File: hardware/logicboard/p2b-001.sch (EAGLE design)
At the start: 54 parts, among them IC1 74LS06N, IC2 4066N, J1 MKR, J2 GPIO, J3 Vcc, J4 RLY, J5 SPI, J7 DIN5, J8 DIN5, J9 DIN5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

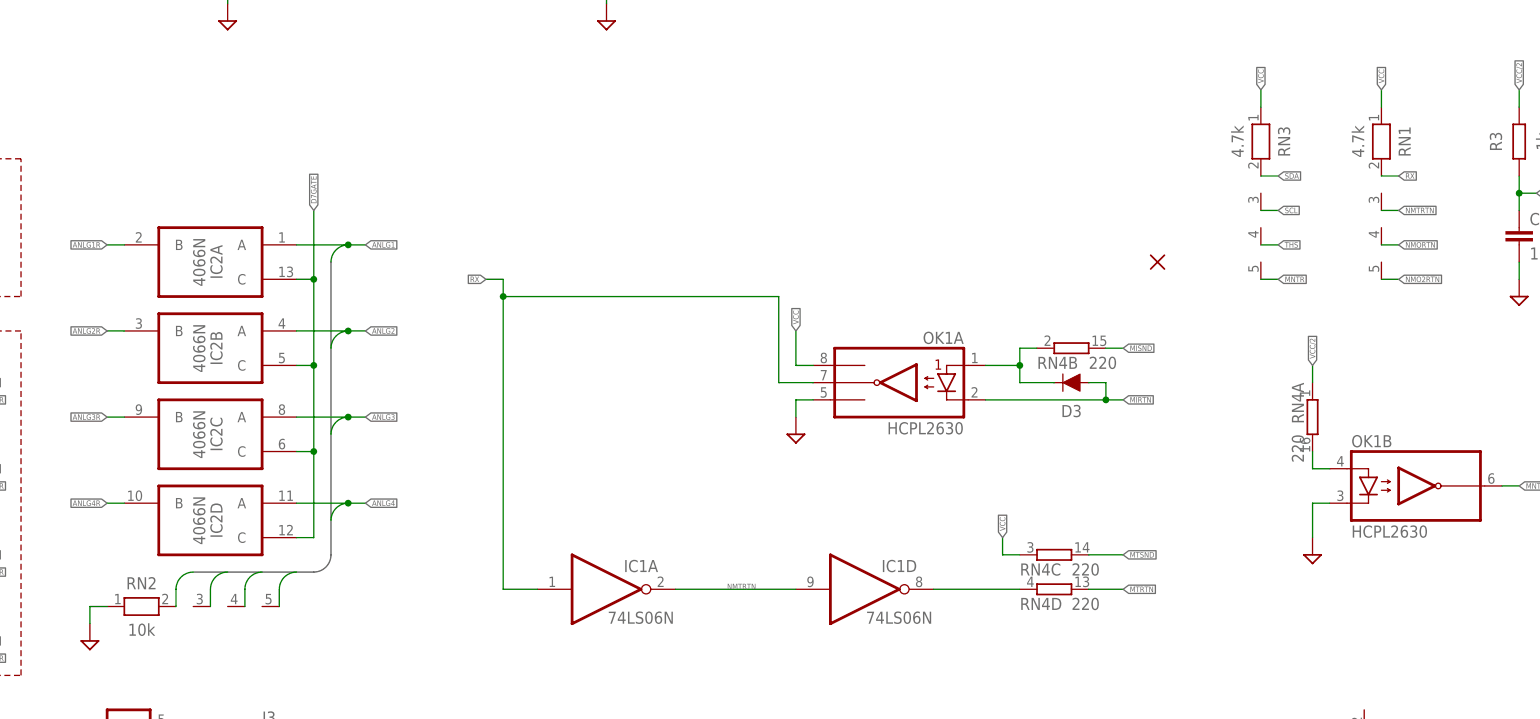
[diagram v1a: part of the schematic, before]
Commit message: Swapped RN1 and RN2.
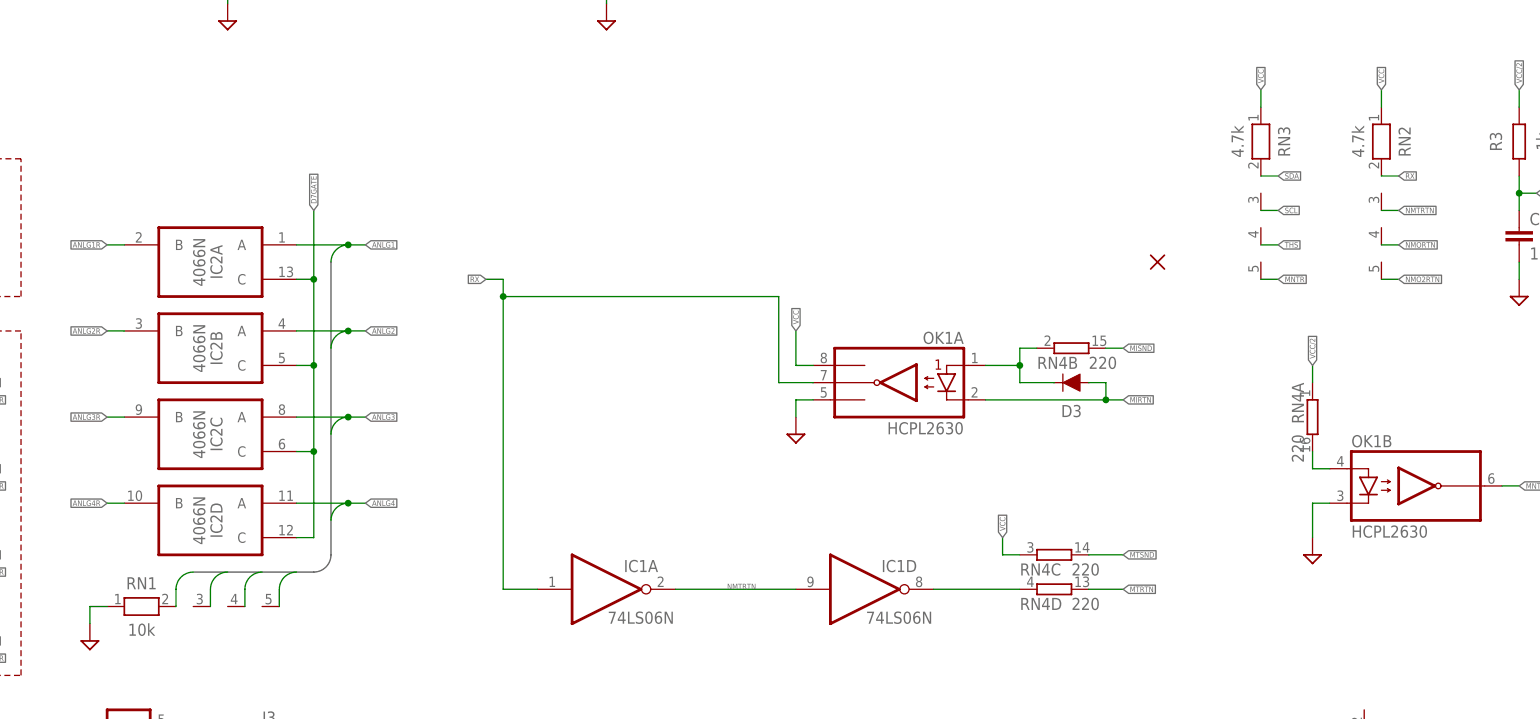
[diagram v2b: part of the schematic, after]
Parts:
- RN1: value 4.7k -> 10k
- RN2: value 10k -> 4.7k
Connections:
- net ANLG1: now also RN1.2; no longer RN2.2
- net ANLG2: now also RN1.3; no longer RN2.3
- net ANLG3: now also RN1.4; no longer RN2.4
- net ANLG4: now also RN1.5; no longer RN2.5
- net GND: now also RN1.1; no longer RN2.1
- net NMO2RTN: now also RN2.5; no longer RN1.5
- net NMORTN: now also RN2.4; no longer RN1.4
- net NMTRTN: now also RN2.3; no longer RN1.3
- net RX: now also RN2.2; no longer RN1.2
- net VCC: now also RN2.1; no longer RN1.1
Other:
- moved on the sheet: RN1, RN2
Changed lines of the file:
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@@
 <part name="R2" library="resistor" library_urn="urn:adsk.eagle:library:348" deviceset="R-EU_" device="0204/5" package3d_urn="urn:adsk.eagle:package:23488/1" value="47k"/>
 <part name="SUPPLY7" library="supply2" deviceset="GND" device=""/>
-<part name="RN2" library="resistor-net" library_urn="urn:adsk.eagle:library:343" deviceset="RN04" device="" package3d_urn="urn:adsk.eagle:package:24976/1" value="10k"/>
+<part name="RN1" library="resistor-net" library_urn="urn:adsk.eagle:library:343" deviceset="RN04" device="" package3d_urn="urn:adsk.eagle:package:24976/1" value="10k"/>
 <part name="IC2" library="40xx" library_urn="urn:adsk.eagle:library:80" deviceset="4066" device="N" package3d_urn="urn:adsk.eagle:package:16407/2"/>
 <part name="SUPPLY26" library="supply2" deviceset="GND" device=""/>
@@
 <part name="C10" library="rcl" library_urn="urn:adsk.eagle:library:334" deviceset="C-EU" device="025-024X044" package3d_urn="urn:adsk.eagle:package:23630/1" value="100n"/>
 <part name="SUPPLY44" library="supply2" deviceset="GND" device=""/>
-<part name="RN1" library="resistor-net" library_urn="urn:adsk.eagle:library:343" deviceset="RN04" device="" package3d_urn="urn:adsk.eagle:package:24976/1" value="4.7k"/>
+<part name="RN2" library="resistor-net" library_urn="urn:adsk.eagle:library:343" deviceset="RN04" device="" package3d_urn="urn:adsk.eagle:package:24976/1" value="4.7k"/>
 <part name="SV1" library="con-ml" library_urn="urn:adsk.eagle:library:164" deviceset="ML16LE" device="" package3d_urn="urn:adsk.eagle:package:8682/1"/>
 <part name="H1" library="SparkFun-Hardware" library_urn="urn:adsk.eagle:library:519" deviceset="STAND-OFF" device="" package3d_urn="urn:adsk.eagle:package:38630/1"/>
@@
 </instance>
 <instance part="SUPPLY7" gate="GND" x="137.16" y="172.72" smashed="yes"/>
-<instance part="RN2" gate="1" x="68.58" y="86.36" smashed="yes">
+<instance part="RN1" gate="1" x="68.58" y="86.36" smashed="yes">
 <attribute name="NAME" x="68.58" y="88.9" size="1.778" layer="95" align="bottom-center"/>
 <attribute name="VALUE" x="68.58" y="83.82" size="1.778" layer="96" align="top-center"/>
@@
 </instance>
 <instance part="SUPPLY44" gate="GND" x="271.78" y="132.08" smashed="yes"/>
-<instance part="RN1" gate="1" x="251.46" y="154.94" smashed="yes" rot="R270">
+<instance part="RN2" gate="1" x="251.46" y="154.94" smashed="yes" rot="R270">
 <attribute name="NAME" x="254" y="154.94" size="1.778" layer="95" rot="R270" align="bottom-center"/>
 <attribute name="VALUE" x="248.92" y="154.94" size="1.778" layer="96" rot="R270" align="top-center"/>
@@
 </segment>
 <segment>
-<pinref part="RN2" gate="1" pin="1"/>
+<pinref part="RN1" gate="1" pin="1"/>
 <wire x1="63.5" y1="86.36" x2="60.96" y2="86.36" width="0.1524" layer="91"/>
 <pinref part="SUPPLY23" gate="GND" pin="GND"/>
@@
 </segment>
 <segment>
-<pinref part="RN1" gate="1" pin="1"/>
+<pinref part="RN2" gate="1" pin="1"/>
 <wire x1="251.46" y1="160.02" x2="251.46" y2="162.56" width="0.1524" layer="91"/>
 <label x="251.46" y="162.56" size="0.8128" layer="95" rot="R90" xref="yes"/>
@@
 </segment>
 <segment>
-<pinref part="RN2" gate="1" pin="5"/>
+<pinref part="RN1" gate="1" pin="5"/>
 <wire x1="91.44" y1="91.44" x2="88.9" y2="88.9" width="0.1524" layer="91" curve="90"/>
 <wire x1="88.9" y1="88.9" x2="88.9" y2="86.36" width="0.1524" layer="91"/>
@@
 </segment>
 <segment>
-<pinref part="RN2" gate="1" pin="4"/>
+<pinref part="RN1" gate="1" pin="4"/>
 <wire x1="86.36" y1="91.44" x2="83.82" y2="88.9" width="0.1524" layer="91" curve="90"/>
 <wire x1="83.82" y1="88.9" x2="83.82" y2="86.36" width="0.1524" layer="91"/>
@@
 </segment>
 <segment>
-<pinref part="RN2" gate="1" pin="3"/>
+<pinref part="RN1" gate="1" pin="3"/>
 <wire x1="81.28" y1="91.44" x2="78.74" y2="88.9" width="0.1524" layer="91" curve="90"/>
 <wire x1="78.74" y1="88.9" x2="78.74" y2="86.36" width="0.1524" layer="91"/>
@@
 </segment>
 <segment>
-<pinref part="RN2" gate="1" pin="2"/>
+<pinref part="RN1" gate="1" pin="2"/>
 <wire x1="76.2" y1="91.44" x2="73.66" y2="88.9" width="0.1524" layer="91" curve="90"/>
 <wire x1="73.66" y1="88.9" x2="73.66" y2="86.36" width="0.1524" layer="91"/>
@@
 </segment>
 <segment>
-<pinref part="RN1" gate="1" pin="2"/>
+<pinref part="RN2" gate="1" pin="2"/>
 <wire x1="251.46" y1="149.86" x2="254" y2="149.86" width="0.1524" layer="91"/>
 <label x="254" y="149.86" size="0.8128" layer="95" xref="yes"/>
@@
 </segment>
 <segment>
-<pinref part="RN1" gate="1" pin="3"/>
+<pinref part="RN2" gate="1" pin="3"/>
 <wire x1="251.46" y1="144.78" x2="254" y2="144.78" width="0.1524" layer="91"/>
 <label x="254" y="144.78" size="0.8128" layer="95" xref="yes"/>
@@
 </segment>
 <segment>
-<pinref part="RN1" gate="1" pin="4"/>
+<pinref part="RN2" gate="1" pin="4"/>
 <wire x1="251.46" y1="139.7" x2="254" y2="139.7" width="0.1524" layer="91"/>
 <label x="254" y="139.7" size="0.8128" layer="95" xref="yes"/>
@@
 </segment>
 <segment>
-<pinref part="RN1" gate="1" pin="5"/>
+<pinref part="RN2" gate="1" pin="5"/>
 <wire x1="251.46" y1="134.62" x2="254" y2="134.62" width="0.1524" layer="91"/>
 <label x="254" y="134.62" size="0.8128" layer="95" xref="yes"/>

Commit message: The new test pad.
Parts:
- removed JP7: (no value), pinhead:PINHD-2X8
- added SV3: (no value), con-ml:ML14E
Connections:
- net D7GATE: now also SV3-7.S; no longer JP7.7
- net DTCT1: now also SV3-11.S; no longer JP7.11
- net DTCT2: now also SV3-12.S; no longer JP7.12
- net DTCT3: now also SV3-13.S; no longer JP7.13
- net DTCT4: now also SV3-14.S; no longer JP7.14
- net GND: now also SV3-1.S; no longer JP7.1
- net GPIO1: now also SV3-9.S; no longer JP7.9
- net GPIO2: now also SV3-10.S; no longer JP7.10
- net LED2: no longer JP7.2
- net MNTR: no longer JP7.15
- net RLY: no longer JP7.8
- net RX: now also SV3-3.S; no longer JP7.3
- net SCL: now also SV3-6.S; no longer JP7.6
- net SDA: now also SV3-5.S; no longer JP7.5
- net THS: now also SV3-8.S; no longer JP7.16
- net TX: now also SV3-4.S; no longer JP7.4
- net VCC: now also SV3-2.S

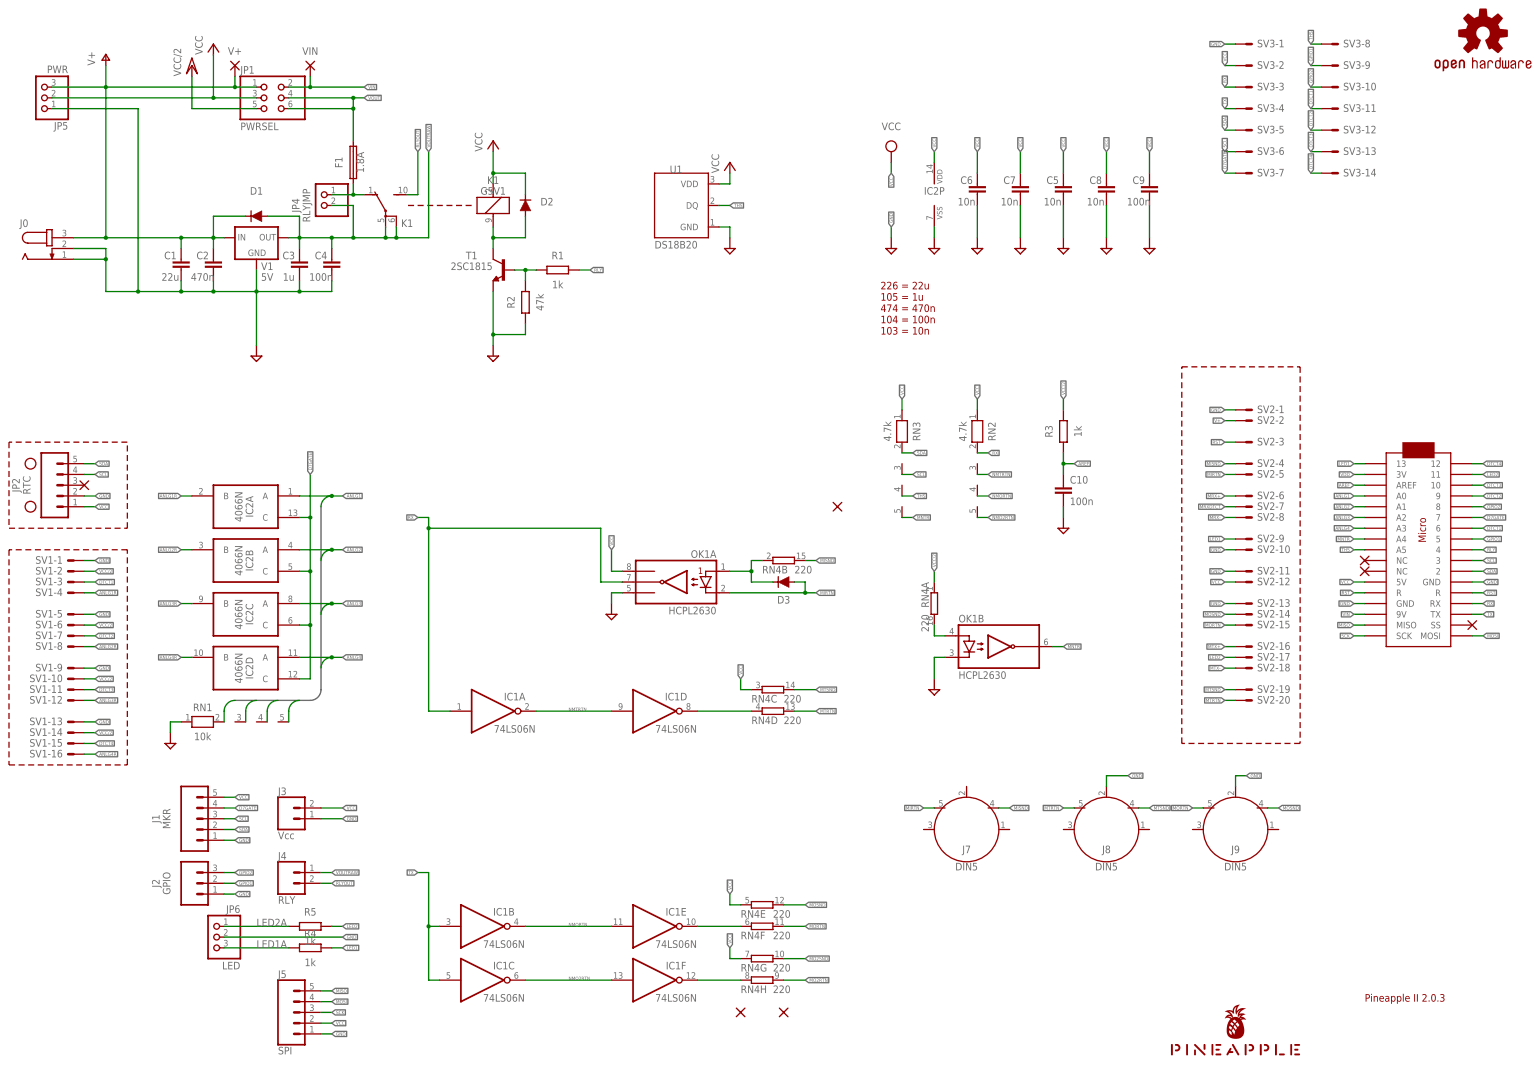
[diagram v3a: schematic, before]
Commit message: Renumbered signal names and silk patterns.
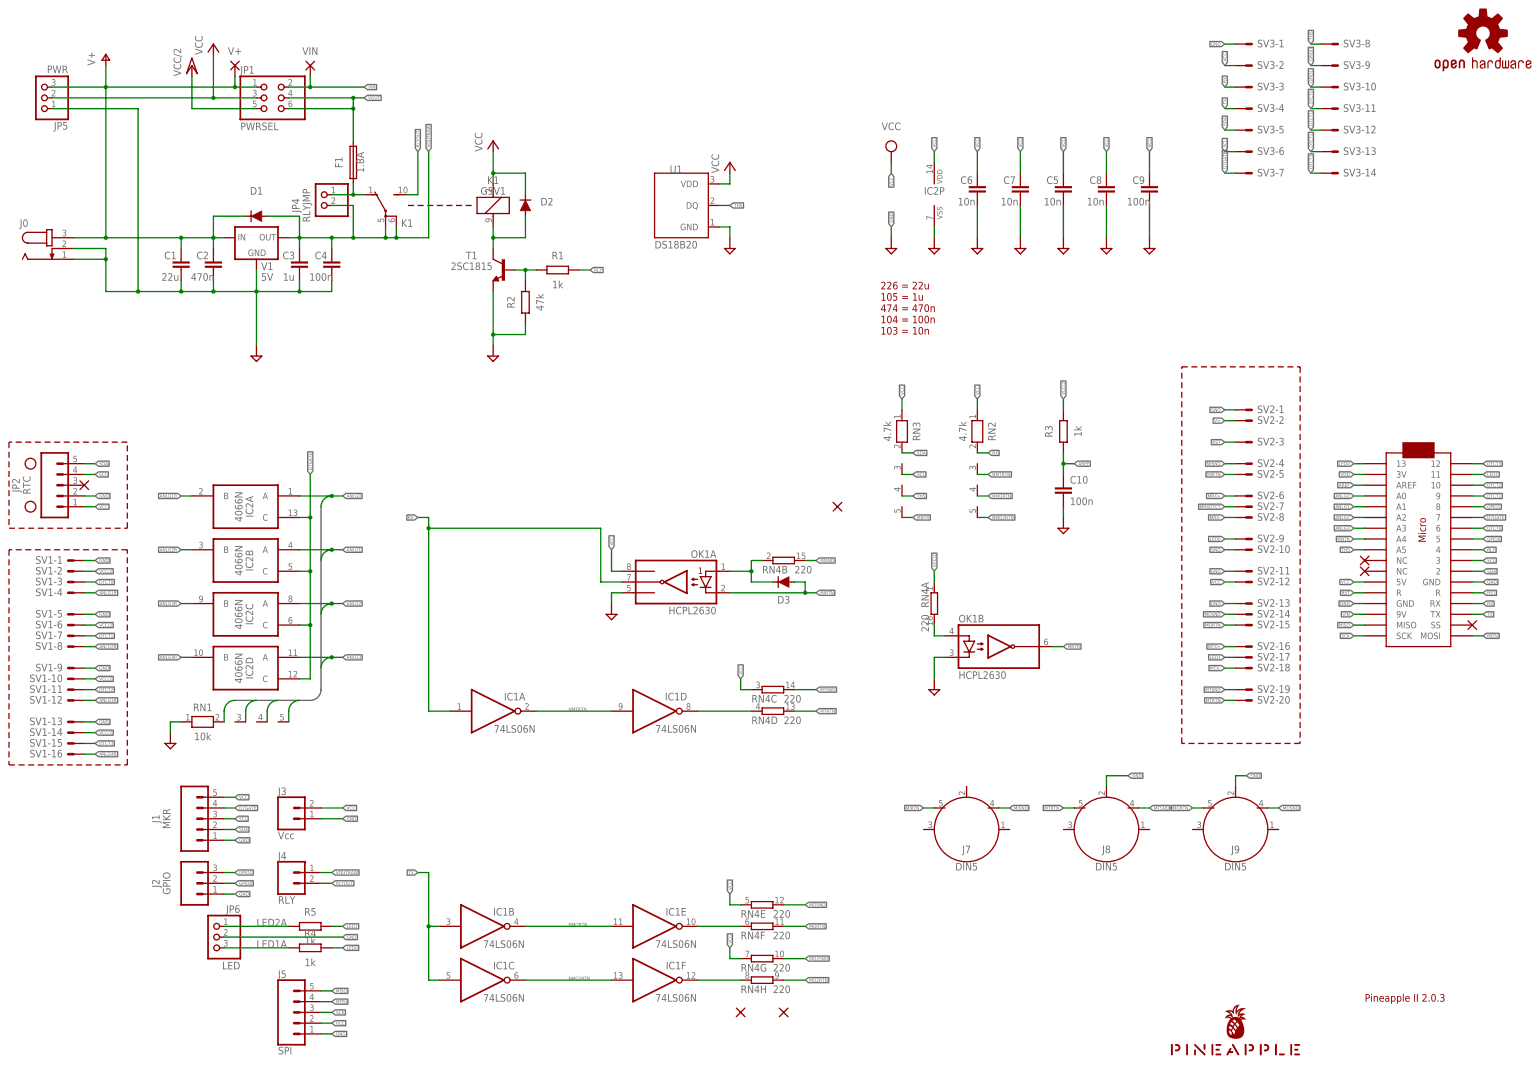
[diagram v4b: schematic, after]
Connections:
- removed net ANLG4: IC2D.A, MC1.A3, RN1.5
- removed net DTCT4: MC1.12, SV1-15.S, SV3-14.S
- removed net GPIO2: J2.3, MC1.8, SV3-10.S
- removed net LED2: MC1.11, R5.2, SV2-17.S
- new net ANLG0: IC2A.A, MC1.A0, RN1.2
- new net DTCT0: MC1.6, SV1-3.S, SV3-11.S
- new net GPIO0: J2.2, MC1.5, SV3-9.S
- new net LED0: MC1.13, R4.2, SV2-9.S
- net ANLG1: now also IC2B.A, MC1.A1, RN1.3; no longer IC2A.A, MC1.A0, RN1.2
- net ANLG2: now also IC2C.A, MC1.A2, RN1.4; no longer IC2B.A, MC1.A1, RN1.3
- net ANLG3: now also IC2D.A, MC1.A3, RN1.5; no longer IC2C.A, MC1.A2, RN1.4
- net DTCT1: now also MC1.9, SV1-7.S, SV3-12.S; no longer MC1.6, SV1-3.S, SV3-11.S
- net DTCT2: now also MC1.10, SV1-11.S, SV3-13.S; no longer MC1.9, SV1-7.S, SV3-12.S
- net DTCT3: now also MC1.12, SV1-15.S, SV3-14.S; no longer MC1.10, SV1-11.S, SV3-13.S
- net GPIO1: now also J2.3, MC1.8, SV3-10.S; no longer J2.2, MC1.5, SV3-9.S
- net LED1: now also MC1.11, R5.2, SV2-17.S; no longer MC1.13, R4.2, SV2-9.S
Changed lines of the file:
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@@
 </segment>
 </net>
-<net name="ANLG4" class="3">
+<net name="ANLG3" class="3">
 <segment>
 <pinref part="MC1" gate="G$1" pin="A3"/>
@@
 </segment>
 </net>
-<net name="ANLG3" class="3">
+<net name="ANLG2" class="3">
 <segment>
 <pinref part="MC1" gate="G$1" pin="A2"/>
@@
 </segment>
 </net>
-<net name="ANLG2" class="3">
+<net name="ANLG1" class="3">
 <segment>
 <pinref part="MC1" gate="G$1" pin="A1"/>
@@
 </segment>
 </net>
-<net name="ANLG1" class="3">
+<net name="ANLG0" class="3">
 <segment>
 <pinref part="MC1" gate="G$1" pin="A0"/>
@@
 </segment>
 </net>
-<net name="DTCT1" class="0">
+<net name="DTCT0" class="0">
 <segment>
 <pinref part="MC1" gate="G$1" pin="6"/>
@@
 </segment>
 </net>
-<net name="DTCT2" class="0">
+<net name="DTCT1" class="0">
 <segment>
 <pinref part="MC1" gate="G$1" pin="9"/>
@@
 </segment>
 </net>
-<net name="DTCT3" class="0">
+<net name="DTCT2" class="0">
 <segment>
 <pinref part="MC1" gate="G$1" pin="10"/>
@@
 </segment>
 </net>
-<net name="DTCT4" class="0">
+<net name="DTCT3" class="0">
 <segment>
 <pinref part="MC1" gate="G$1" pin="12"/>
@@
 </segment>
 </net>
-<net name="LED1" class="0">
+<net name="LED0" class="0">
 <segment>
 <pinref part="MC1" gate="G$1" pin="13"/>
@@
 </segment>
 </net>
-<net name="LED2" class="0">
+<net name="LED1" class="0">
 <segment>
 <pinref part="MC1" gate="G$1" pin="11"/>
@@
 </segment>
 </net>
-<net name="GPIO2" class="0">
+<net name="GPIO1" class="0">
 <segment>
 <pinref part="MC1" gate="G$1" pin="8"/>
@@
 </segment>
 </net>
-<net name="GPIO1" class="0">
+<net name="GPIO0" class="0">
 <segment>
 <pinref part="MC1" gate="G$1" pin="5"/>
